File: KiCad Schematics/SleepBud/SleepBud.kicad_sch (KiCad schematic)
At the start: 135 parts, among them J1 USB_B_Micro, J2 12V Barrel Jack, Q1 AO3400A, Q2 FQP27P06, SW1 Mode Button, SW2 Up Button, SW3 Down Button, SW4 EN Button, SW5 Switch Button, SW6 Reset Button, U1 ESP32-S3-WROOM-1, U2 DS3231SN_, U3 PIR, U4 AMS1117-3.3, U5 AMS1117-5.0, U6 TXS0108EPW, U7 Lamp SMD

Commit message: Switched some footprints and schematics
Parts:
- removed SW1: Mode Button, Button_Switch_SMD:SW_SPST_B3S-1000, symbol Switch:SW_Push
- removed SW2: Up Button, Button_Switch_SMD:SW_SPST_B3S-1000, symbol Switch:SW_Push
- removed SW3: Down Button, Button_Switch_SMD:SW_SPST_B3S-1000, symbol Switch:SW_Push
- removed SW5: Switch Button, Button_Switch_SMD:SW_SPST_B3S-1000, symbol Switch:SW_Push
- removed U3: PIR, Connector_PinHeader_1.00mm:PinHeader_1x03_P1.00mm_Vertical_SMD_Pin1Left, symbol AMC312_Mini_PIR:AM312
- removed U7: Lamp SMD, Connector_PinHeader_1.00mm:PinHeader_1x03_P1.00mm_Vertical_SMD_Pin1Right, symbol LampSignals:Lamp_Power
- added D79: ~, symbol WS2812B Pads:WS21812B_Pads
- added J3: 1984798, 1984798:CONN_1984798_PXC, symbol 2024-11-07_22-19-03:1984798
- added J4, J5: 1984772, 1984772:CONN_1984772_PXC, symbol 2024-11-07_22-38-37:1984772
- J1: renamed from J2; footprint Connector_BarrelJack:BarrelJack_Wuerth_694108106102_2.5x5.5mm -> 1984769:CONN_1984769_PXC
- R13: renamed from R4; footprint Resistor_SMD:R_0201_0603Metric -> Resistor_SMD:R_0603_1608Metric
- renumbered C9 to C10, C14 to C11, C13 to C12, C10 to C13, C11 to C14, C6 to C5, C7 to C6, C5 to C7, C12 to C8, C8 to C9, D17 to D1, D4 to D10, D5 to D11, D6 to D12, D26 to D13, D27 to D14, D22 to D15, D23 to D16, D7 to D17, D8 to D18, D9 to D19, D18 to D2, D10 to D20, D11 to D21, D28 to D22, D29 to D23, D12 to D24, D13 to D25, D14 to D26, D15 to D27, D16 to D28, D30 to D29, D19 to D3, D31 to D30, D46 to D31, D47 to D32, D48 to D33, D49 to D34, D50 to D35, D51 to D36, D52 to D37, D53 to D38, D54 to D39, D20 to D4, D55 to D40, D56 to D41, D57 to D42, D1 to D43, D32 to D44, D33 to D45, D34 to D46, D35 to D47, D36 to D48, D37 to D49, D21 to D5, D38 to D50, D39 to D51, D40 to D52, D41 to D53, D42 to D54, D43 to D55, D44 to D56, D45 to D57, D24 to D6, D25 to D7, D2 to D8, D3 to D9, J1 to J2, JP3 to JP2, JP2 to JP3, Q2 to Q1, Q1 to Q2, R20 to R10, R14 to R11, R15 to R12, R8 to R14, R2 to R15, R12 to R16, R9 to R17, R13 to R18, R10 to R19, R5 to R2, R11 to R20, R16 to R4, R6 to R5, R17 to R6, R18 to R7, R7 to R8, R19 to R9, SW4 to SW1, SW6 to SW2, U4 to U1, U5 to U2, U1 to U3, U2 to U4, U6 to U5
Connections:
- net +3.3V: now also J4.1; no longer U4.15 (SDA), U4.16 (SCL)
- net +5V: now also J5.1
- net GND: now also J3.1, J4.3, J5.3
- net at R12.2, U3.29 (IO36): now also U4.15 (SDA)
- net at R6.2, U3.4 (IO4): now also J3.5
- net at R7.2, U3.5 (IO5): now also J3.4
- net at R10.2, U3.7 (IO7): now also J3.2
- net at R9.2, U3.6 (IO6): now also J3.3
- net at R11.2, U3.28 (IO35): now also U4.16 (SCL)
- net at U3.12 (IO8): now also J4.2
- net at R15.2: now also J5.2
- net LED Lamp: no longer names the net of R15.1, U5.20 (B1)
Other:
- note added: "Connected to External Buttons"
- note added: "Down"
- note added: "LED Lamp Holder"
- note added: "Mode"
- note added: "Switch"
- note added: "Up"
- note removed: "Buttons"
- moved on the sheet: C1, C2, C3, C4, CR1, D1, D10, D11, D12, D13, D14, D15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

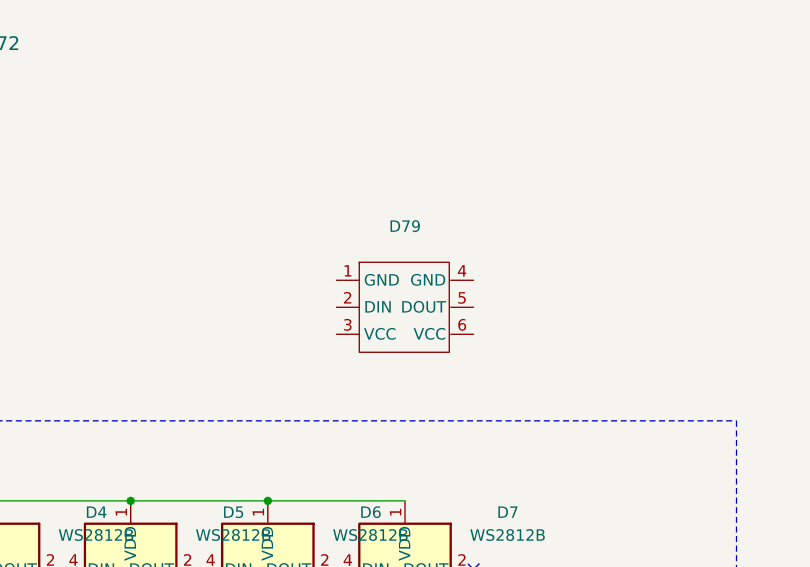
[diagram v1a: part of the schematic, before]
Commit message: Updated Footprints
Footprint for WB2812B LED was personalized
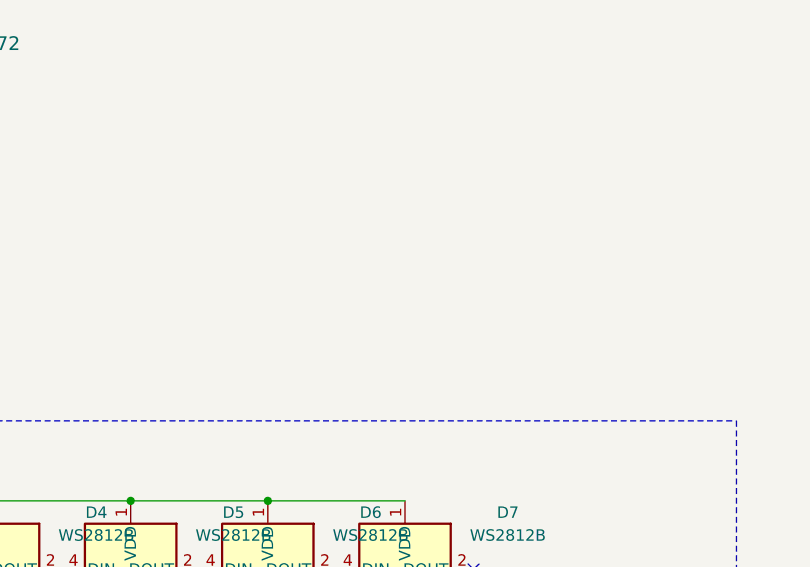
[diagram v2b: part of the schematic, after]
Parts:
- removed D79: ~, symbol WS2812B Pads:WS21812B_Pads
- D1: footprint LED_SMD:LED_WS2812B_PLCC4_5.0x5.0mm_P3.2mm -> Custom:WB2812B
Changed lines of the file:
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@@
 	)
 	(symbol
+		(lib_name "WS2812B_1")
 		(lib_id "LED:WS2812B")
 		(at 321.31 190.5 0)
@@
 			)
 		)
-		(property "Footprint" "LED_SMD:LED_WS2812B_PLCC4_5.0x5.0mm_P3.2mm"
+		(property "Footprint" "Custom:WB2812B"
 			(at 322.58 198.12 0)
 			(effects
@@
 					(unit 1)
 				)
-			)
-		)
-	)
-	(symbol
-		(lib_id "WS2812B Pads:WS21812B_Pads")
-		(at 407.67 166.37 0)
-		(unit 1)
-		(exclude_from_sim no)
-		(in_bom yes)
-		(on_board yes)
-		(dnp no)
-		(fields_autoplaced yes)
-		(property "Reference" "D79"
-			(at 412.75 152.4 0)
-			(effects
-				(font
-					(size 1.27 1.27)
-				)
-			)
-		)
-		(property "Value" "~"
-			(at 412.75 154.94 0)
-			(effects
-				(font
-					(size 1.27 1.27)
-				)
-			)
-		)
-		(property "Footprint" ""
-			(at 407.67 166.37 0)
-			(effects
-				(font
-					(size 1.27 1.27)
-				)
-				(hide yes)
-			)
-		)
-		(property "Datasheet" ""
-			(at 407.67 166.37 0)
-			(effects
-				(font
-					(size 1.27 1.27)
-				)
-				(hide yes)
-			)
-		)
-		(property "Description" ""
-			(at 407.67 166.37 0)
-			(effects
-				(font
-					(size 1.27 1.27)
-				)
-				(hide yes)
-			)
-		)
-		(pin "4"
-		)
-		(pin "3"
-		)
-		(pin "2"
-		)
-		(pin "5"
-		)
-		(pin "1"
-		)
-		(pin "6"
-		)
-		(instances
-			(project ""
-				(path "/976e55d6-47c8-4a6a-a3ac-d81121411704"
-					(reference "D79")
-					(unit 1)
-				)

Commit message: just moved some stuff around and changed some texts
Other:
- note added: "Connected to 4 External Buttons"
- note added: "LED Lamp Connector"
- note removed: "Connected to External Buttons"
- note removed: "LED Lamp Holder"
- note removed: "Not sure if correct"
- moved on the sheet: BT1, BZ1, C1, C10, C11, C12, C13, C14, C2, C3, C4, C5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

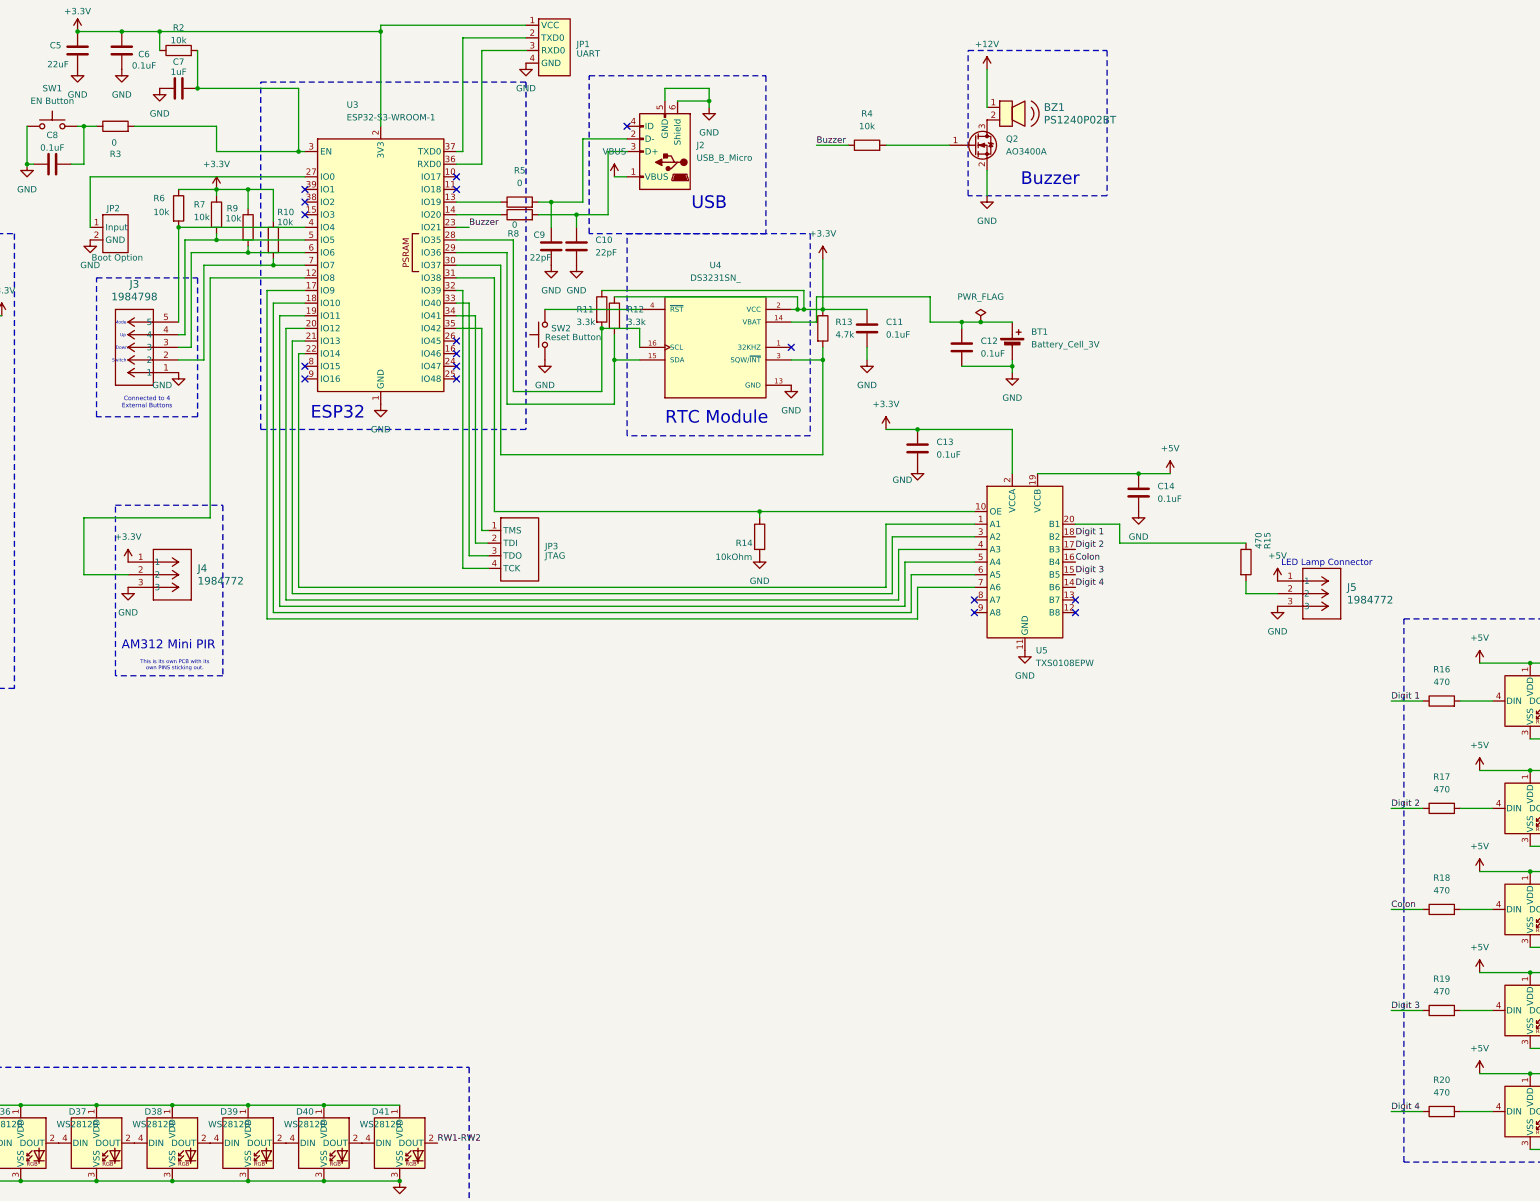
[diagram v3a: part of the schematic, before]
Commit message: Placed Parts to Potential area on Layout
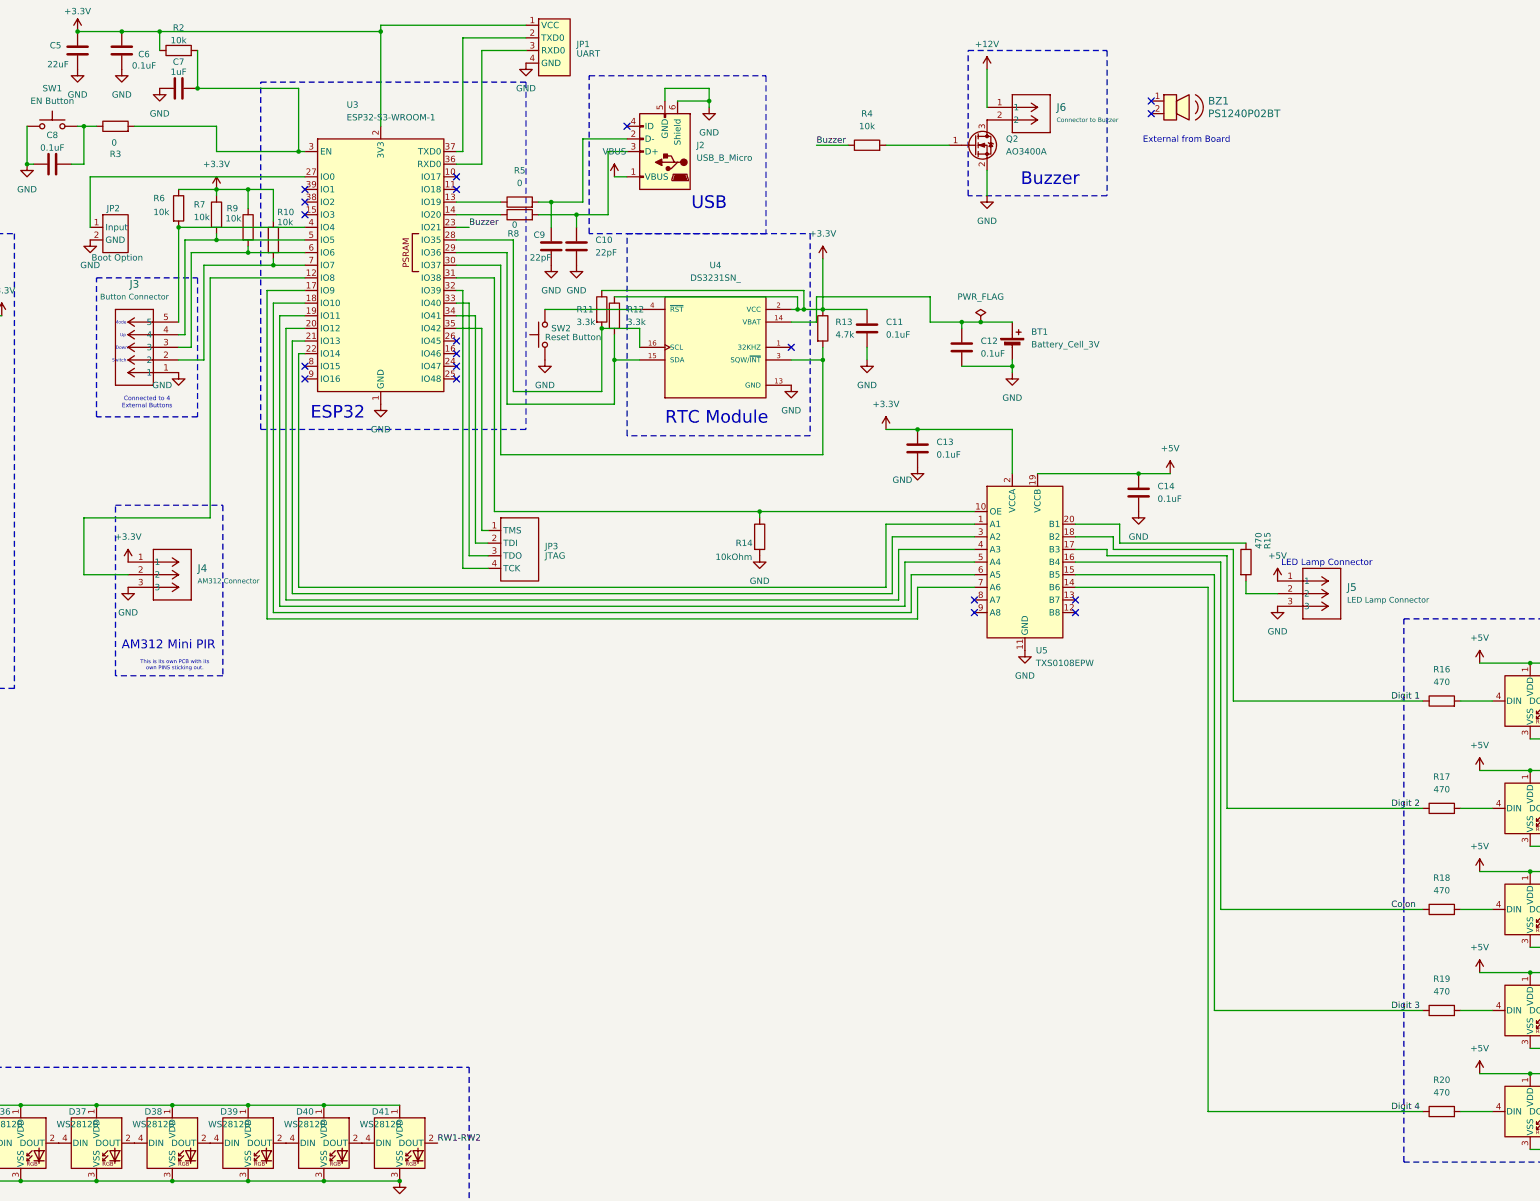
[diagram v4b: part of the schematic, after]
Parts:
- added J6: Connector to Buzzer, 1984769:CONN_1984769_PXC, symbol 2024-11-07_22-48-53:1984769
- D1: footprint Custom:WB2812B -> Custom Pads:WB2812B
- D10, D11, D12, D13, D14, D15, D16, D17, D18, D19, D2, D20, D21, D22, D23, D24, D25, D26, D27, D28, D29, D3, D30, D4, D5, D6, D7, D8, D9: footprint LED_SMD:LED_WS2812B_PLCC4_5.0x5.0mm_P3.2mm -> Custom Pads:WB2812B
- J3: value 1984798 -> Button Connector
- J4: value 1984772 -> AM312 Connector
- J5: value 1984772 -> LED Lamp Connector
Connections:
- net +12V: now also J6.1; no longer BZ1.1
- net at Q2.3 (D): now also J6.2; no longer BZ1.2
- no-connect marks 24 -> 26
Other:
- note added: "External from Board"
- moved on the sheet: BZ1

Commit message: Back of PCB Almost Done, Started on Front
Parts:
- BT1: footprint Battery:BatteryHolder_Keystone_1057_1x2032 -> BH74G5P:BH-74G-5-P_ADM
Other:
- note removed: "can change diode if need be"
- note removed: "prob change mosfet that can be smd"
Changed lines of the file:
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@@
 		)
 	)
-	(text "can change diode if need be"
-		(exclude_from_sim no)
-		(at 70.104 156.464 0)
-		(effects
-			(font
-				(size 0.635 0.635)
-			)
-		)
-	)
 	(text "AM312 Mini PIR"
 		(exclude_from_sim no)
@@
 		)
 	)
-	(text "prob change mosfet that can be smd"
-		(exclude_from_sim no)
-		(at 81.534 137.668 0)
-		(effects
-			(font
-				(size 0.508 0.508)
-			)
-		)
-	)
 	(text "Other Side of the PCB Board\n"
 		(exclude_from_sim no)
@@
 			)
 		)
-		(property "Footprint" "Battery:BatteryHolder_Keystone_1057_1x2032"
+		(property "Footprint" "BH74G5P:BH-74G-5-P_ADM"
 			(at 323.85 153.416 90)
 			(effects

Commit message: PCB Layout Routing Rough Draft Finished
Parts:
- U2: value AMS1117-5.0 -> AZ1084CD; footprint Package_TO_SOT_SMD:SOT-223-3_TabPin2 -> Custom Pads:AZ1084CD
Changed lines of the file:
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@@
 			)
 		)
-		(property "Value" "AMS1117-5.0"
+		(property "Value" "AZ1084CD"
 			(at 85.09 195.58 0)
 			(effects
@@
 			)
 		)
-		(property "Footprint" "Package_TO_SOT_SMD:SOT-223-3_TabPin2"
+		(property "Footprint" "Custom Pads:AZ1084CD"
 			(at 85.09 194.31 0)
 			(effects

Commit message: Fixed all violations on PCB
Just need to work on grounding parts, and switching mosfets, adding connections
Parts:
- added SW3: Mode Button, symbol Switch:SW_Push
- added SW4: Up Button, symbol Switch:SW_Push
- added SW5: Down Button, symbol Switch:SW_Push
- added SW6: Switch Button, symbol Switch:SW_Push
- added TP1, TP10, TP11, TP12, TP13, TP14, TP15, TP2, TP22, TP3, TP4, TP5, TP6, TP7, TP8, TP9: TestPoint_Flag, Custom Pads:Testpoint Pad, symbol Connector:TestPoint_Flag
- added TP16, TP17, TP18, TP19, TP20, TP21: TestPoint_Small, Custom Pads:Testpoint Pad, symbol Connector:TestPoint_Small
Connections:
- net +12V: now also TP6.1; no longer J6.1
- net +3.3V: now also TP8.1
- net +5V: now also J6.1, TP7.1
- net VBUS: now also TP10.1
- net IO36-SDA: now reaches R12.2, U3.29 (IO36), U4.15 (SDA)
- net IO36-SDA: now also TP14.1
- net IO38-OE: now reaches R14.1, U3.31 (IO38), U5.10 (OE)
- net at Q2.1 (G), R4.2: now also TP12.1
- net IO35-SCL: now reaches R11.2, U3.28 (IO35), U4.16 (SCL)
- net IO35-SCL: now also TP13.1
- net IO14 - A1: now reaches U3.22 (IO14), U5.1 (A1)
- net IO14 - A1: now also TP16.1
- net IO13 - A2: now reaches U3.21 (IO13), U5.3 (A2)
- net IO13 - A2: now also TP17.1
- net IO12 - A3: now reaches U3.20 (IO12), U5.4 (A3)
- net IO12 - A3: now also TP18.1
- net IO11 - A4: now reaches U3.19 (IO11), U5.5 (A4)
- net IO11 - A4: now also TP19.1
- net IO10 - A5: now reaches U3.18 (IO10), U5.6 (A5)
- net IO10 - A5: now also TP20.1
- net IO9 - A6: now reaches U3.17 (IO9), U5.7 (A6)
- net IO9 - A6: now also TP21.1
- net IO37-SQW/INT: now reaches R13.2, U3.30 (IO37), U4.3 (SQW/~{INT})
- net IO37-SQW/INT: now also TP15.1
- net at C1.1, CR1.1, Q1.3 (S)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: now also TP9.1
- net at BT1.1 (+), C12.1, U4.14 (VBAT): now also TP22.1
- net IO8 - Output2: now reaches J4.2, U3.12 (IO8)
- net IO8 - Output2: now also TP11.1
- net Colon renamed B4 - Colon
- net B4 - Colon: now also TP3.1
- net Digit 1 renamed B2 - Digit 1
- net B2 - Digit 1: now also TP5.1
- net Digit 2 renamed B3 - Digit 2
- net B3 - Digit 2: now also TP4.1
- net Digit 3 renamed B5 - Digit 3
- net B5 - Digit 3: now also TP2.1
- net Digit 4 renamed B6 - Digit 4
- net B6 - Digit 4: now also TP1.1
- no-connect marks 26 -> 34
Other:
- note added: "External Buttons (Not on PCB)"
- note added: "Version 1.3"
- note removed: "Version 1.2"
- moved on the sheet: C1, C2, C3, C4, CR1, D31, D32, D33, D34, D35, D36, D37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
